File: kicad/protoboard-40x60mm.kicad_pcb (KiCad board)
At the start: 2 copper layers, 60 x 40 mm, 1057 parts

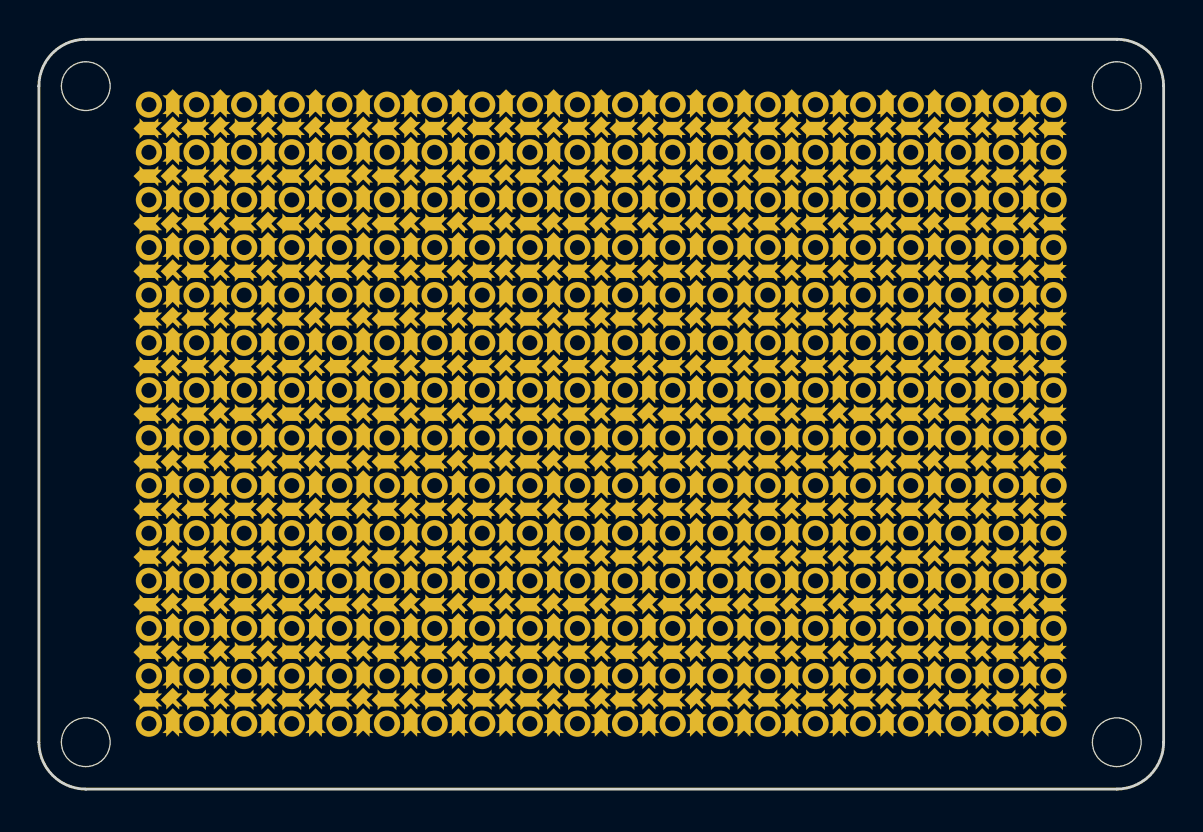
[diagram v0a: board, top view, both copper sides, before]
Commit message: Prettify 40x60 standard PCB
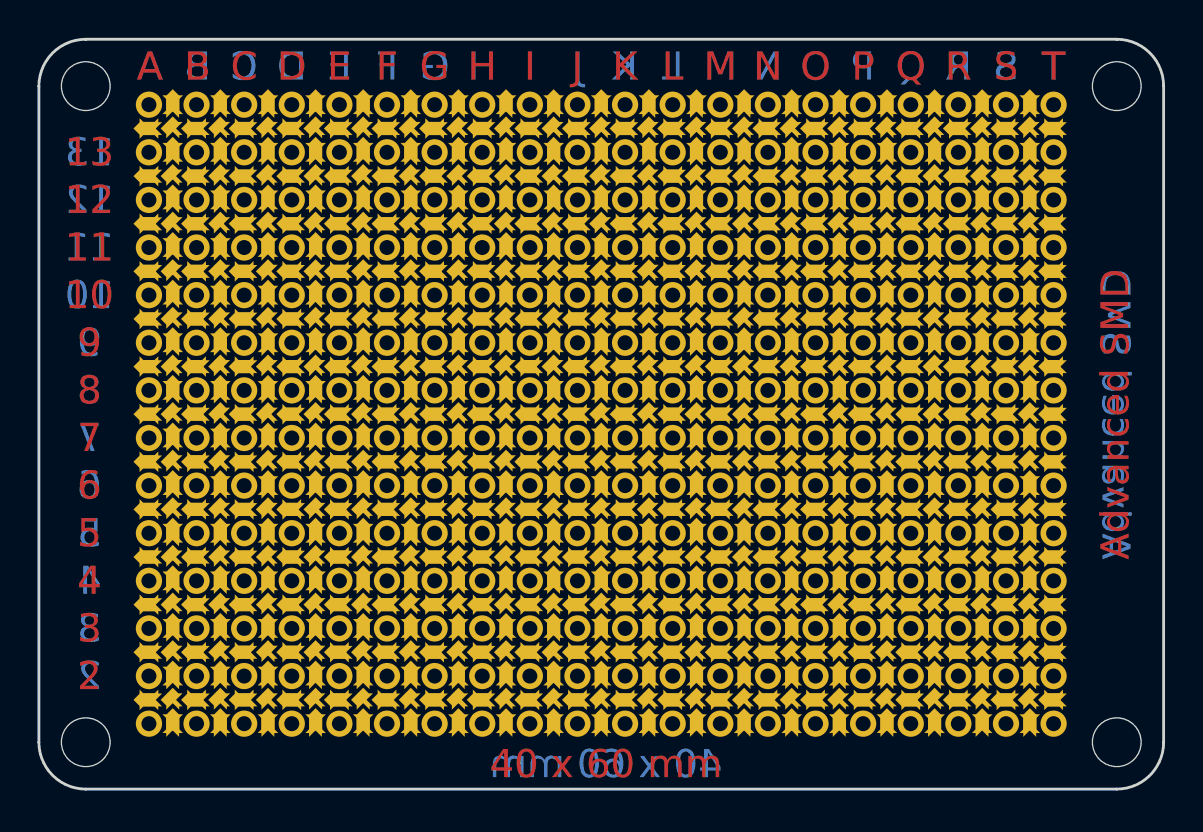
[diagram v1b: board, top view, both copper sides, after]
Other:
- board text added: "10"
- board text added: "11"
- board text added: "12"
- board text added: "13"
- board text added: "2"
- board text added: "3"
- board text added: "4"
- board text added: "40 x 60 mm"
- board text added: "5"
- board text added: "6"
- board text added: "7"
- board text added: "8"
- board text added: "9"
- board text added: "A"
- board text added: "Advanced SMD"
- board text added: "B"
- board text added: "C"
- board text added: "D"
- board text added: "E"
- board text added: "F"
- board text added: "G"
- board text added: "H"
- board text added: "I"
- board text added: "J"
- board text added: "K"
- board text added: "L"
- board text added: "M"
- board text added: "N"
- board text added: "O"
- board text added: "P"
- board text added: "Q"
- board text added: "R"
- board text added: "S"
- board text added: "T"
